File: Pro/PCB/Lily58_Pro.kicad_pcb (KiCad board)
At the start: 2 copper layers, 142.5 x 106.3 mm, 87 parts, among them J1 LED, J2 4PIN, J3 OLED, P1 i2c_pin, P2 i2c_pin, SW1 SW_PUSH, SW10 SW_PUSH, SW11 SW_PUSH, SW12 SW_PUSH, SW13 SW_PUSH, SW14 SW_PUSH, SW15 SW_PUSH, SW16 SW_PUSH, SW17 SW_PUSH, SW18 SW_PUSH, SW19 SW_PUSH, SW2 SW_PUSH, SW20 SW_PUSH, SW21 SW_PUSH, SW22 SW_PUSH, SW23 SW_PUSH, SW24 SW_PUSH, SW25 SW_PUSH, SW26 SW_PUSH, SW27 SW_PUSH, SW28 SW_PUSH, SW29 SW_PUSH, SW3 SW_PUSH, SW4 SW_PUSH, SW5 SW_PUSH, SW6 SW_PUSH, SW7 SW_PUSH, SW8 SW_PUSH, SW9 SW_PUSH, U1 ProMicro

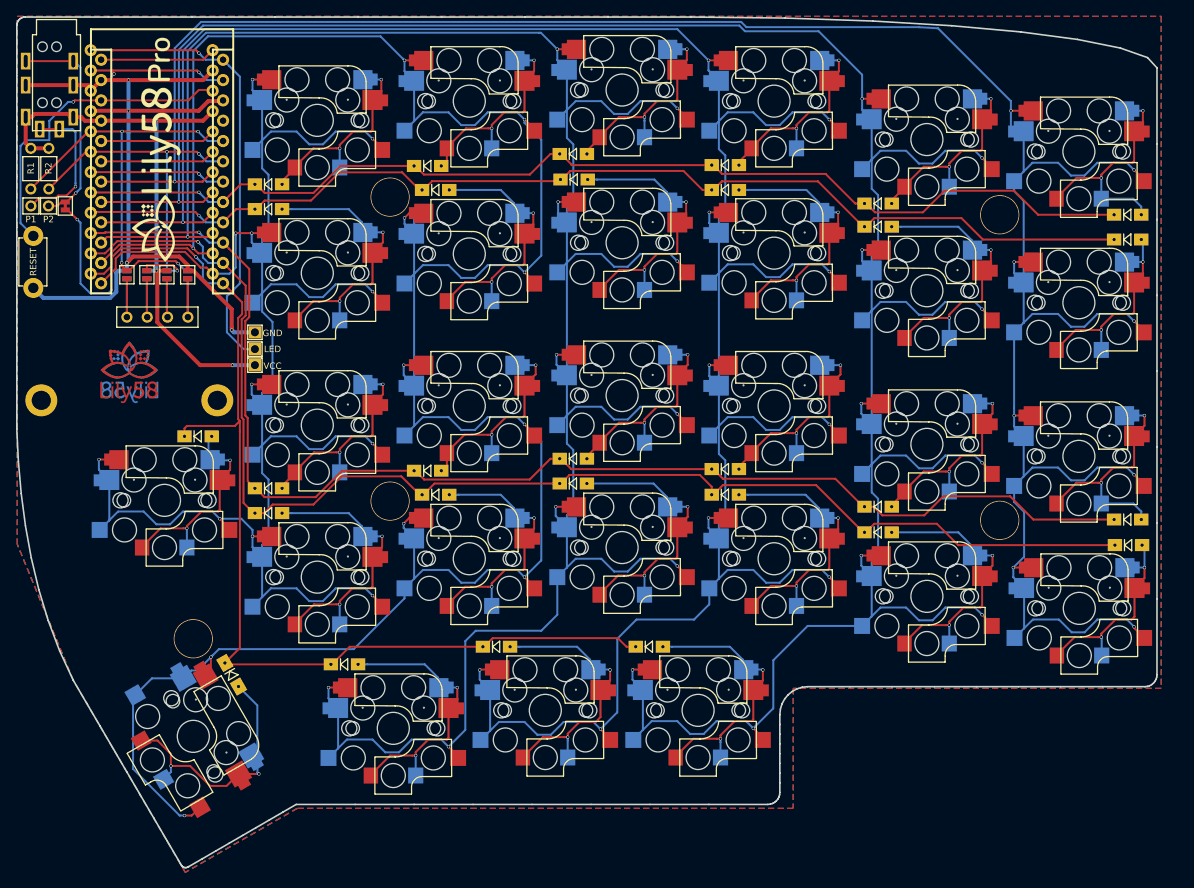
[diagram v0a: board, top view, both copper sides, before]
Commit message: Update project according KiCAD 7
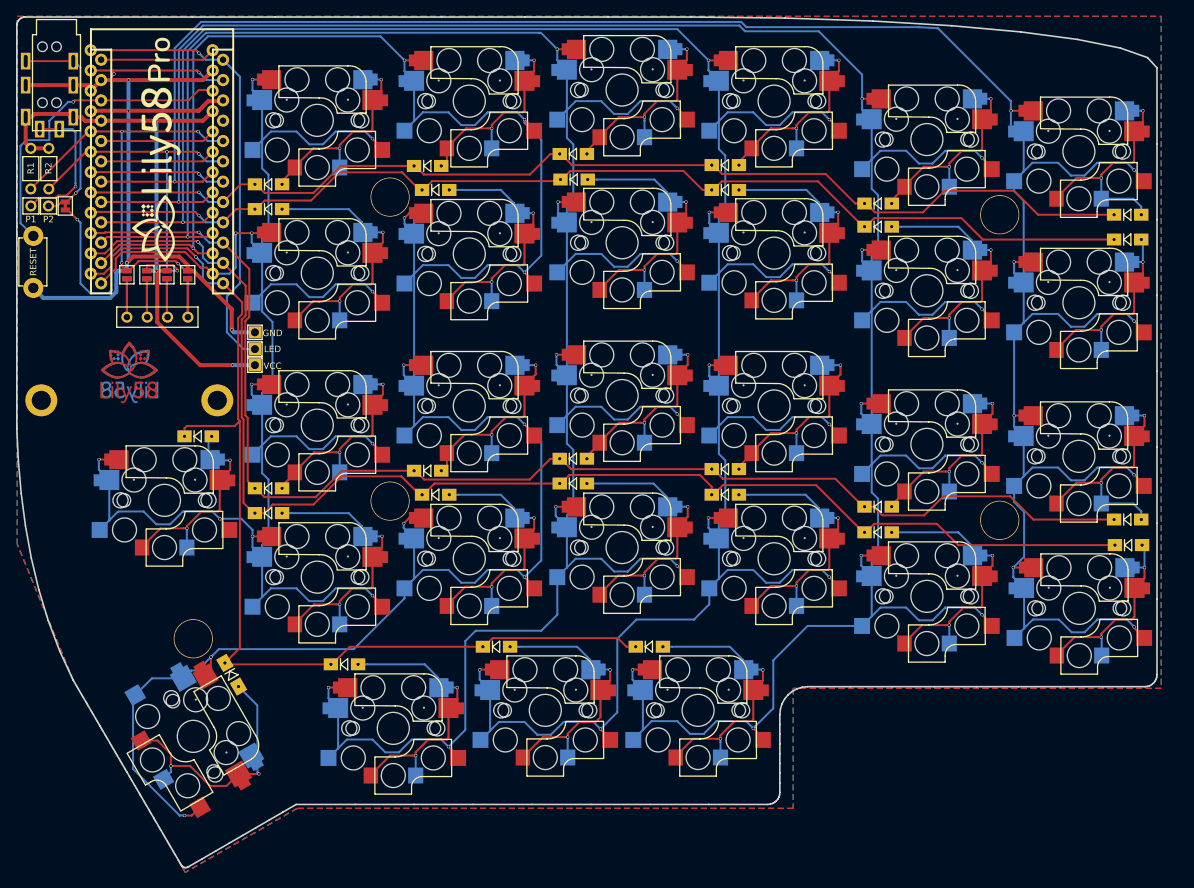
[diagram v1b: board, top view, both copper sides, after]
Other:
- net class Default removed
- net class GND removed
- net class VCC removed

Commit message: wireless scheme is almost ready
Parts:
- removed G*** (x2): LOGO, Lily58-footprint:lily58_logo_Pro
- removed G*** (x2): LOGO, Lily58-footprint:lily58_logo_2
- removed P1, P2: i2c_pin, Lily58-footprint:1pin_conn
- removed R1, R2: R, Lily58-footprint:RESISTOR_mini
- removed W1: jumper, Lily58-footprint:jumper_data
- added JP10: ~, Lily58_Pro:Jumper, B.Cu at (87.6, 61.6)
- added JP11: ~, Lily58_Pro:Jumper, F.Cu at (87.6, 61.6)
- added JP12: ~, Lily58_Pro:Jumper, F.Cu at (85.6, 61.6)
- added JP9: ~, Lily58_Pro:Jumper, B.Cu at (85.6, 61.6)
- added SW30: FS_SW_SPDT, marbastlib-various:SW_MSK12C02-HB, F.Cu at (84.6, 53.7)
- added SW31: BS_SW_SPDT, marbastlib-various:SW_MSK12C02-HB, B.Cu at (84.6, 53.7)
- D1, D10, D11, D12, D13, D14, D15, D16, D17, D18, D19, D2, D20, D21, D22, D23, D24, D25, D26, D27, D28, D29, D3, D4, D5, D6, D7, D8, D9: footprint Lily58-footprint:Diode_SOD123 -> Lily58_Pro:Diode_TH_SOD123
- J1: value LED -> FS_Battery_Socket; footprint Lily58-footprint:LED -> Connector_JST:JST_PH_S2B-PH-K_1x02_P2.00mm_Horizontal
- J2: value 4PIN -> BS_Battery_Socket; footprint Lily58-footprint:MJ-4PP-9 -> Connector_JST:JST_PH_S2B-PH-K_1x02_P2.00mm_Horizontal; moved to B.Cu
- J3: footprint Lily58-footprint:OLED_4Pin -> Lily58_Pro:OLED_4Pin
- JP1, JP2, JP3, JP4, JP5, JP6, JP7, JP8: value (none) -> Jumper_NO_Small; footprint Lily58-footprint:Jumper -> Lily58_Pro:Jumper
- RSW1: footprint Lily58-footprint:TACT_SWITCH_TVBP06 -> Lily58_Pro:TACT_SWITCH_TVBP06
- SW1, SW10, SW11, SW12, SW13, SW14, SW15, SW16, SW17, SW18, SW19, SW2, SW20, SW21, SW22, SW23, SW24, SW25, SW26, SW27, SW28, SW29, SW3, SW4, SW5, SW6, SW7, SW8, SW9: footprint Lily58-footprint:CherryMX_KailhLowProfile_Hotswap_edge -> Lily58_Pro:MX_Choc_Hotswap
- TH1, TH2: footprint Lily58-footprint:M2_HOLE_PCB -> Lily58_Pro:HOLE_M2
- TH3, TH4, TH5, TH6, TH7: footprint Lily58-footprint:HOLE_M2_TH -> Lily58_Pro:HOLE_M2_TH
- U1: footprint Lily58-footprint:ProMicro_rev2 -> Lily58_Pro:ProMicro_rev2
- moved J1 31.8 mm to (85.6, 64.5), turned to 0 degrees
- moved J2 25.2 mm to (87.6, 64.5), turned to 180 degrees
- moved RSW1 24.1 mm to (85.9, 43.6), turned to -90 degrees
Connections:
- J1 pad 1: VCC -> Net-(J1-Pin_1)
- J1 pad 2: LED -> Net-(J1-Pin_1)
- J2 pad 1: VCC -> Net-(J1-Pin_1)
- J2 pad 2: GND -> Net-(J1-Pin_1)
- U1 pad 1: LED -> unconnected-(U1-TX(PD3)-Pad1)
- U1 pad 19: Net-(U1-Pad19) -> unconnected-(U1-A2(PF5)-Pad19)
- U1 pad 20: Net-(U1-Pad20) -> unconnected-(U1-A3(PF4)-Pad20)
- U1 pad 24: Net-(U1-Pad24) -> RAW
- U1 pad 7: Net-(U1-Pad7) -> unconnected-(U1-D4(PD4)-Pad7)
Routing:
- net (no net): track 0.00 -> 414.3 mm, vias 0 -> 23
- net LED: track 57.0 -> 0.00 mm, vias 1 -> 0
- net DATA: track 59.7 -> 17.0 mm, vias 3 -> 1
- net Net-(D7-A): track 37.3 -> 0.00 mm, vias 2 -> 0
- net Net-(D19-A): track 37.2 -> 0.00 mm, vias 2 -> 0
- net Net-(D21-A): track 37.2 -> 0.00 mm, vias 2 -> 0
- net Net-(D23-A): track 37.1 -> 0.00 mm, vias 2 -> 0
- net Net-(D28-A): track 37.1 -> 0.00 mm, vias 2 -> 0
- net Net-(D22-A): track 37.1 -> 0.00 mm, vias 2 -> 0
- net Net-(D11-A): track 37.1 -> 0.00 mm, vias 2 -> 0
- net Net-(D10-A): track 37.0 -> 0.00 mm, vias 2 -> 0
- net VCC: track 72.9 -> 35.9 mm, vias 3 -> 2
- net Net-(D9-A): track 36.9 -> 0.00 mm, vias 2 -> 0
- net RAW: track 0.00 -> 36.9 mm, vias 0 -> 1
- net Net-(D8-A): track 35.0 -> 0.00 mm, vias 2 -> 0
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- removed copper zone on B.Cu, net GND
- removed copper zone on F.Cu, net GND
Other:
- outline, holes or cut-outs redrawn

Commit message: itermediate version
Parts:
- added G***: LOGO, Lily58_Pro:Hedgehog, B.Cu at (95.8, 82.0)
- added LOGO: LOGO, Lily58_Pro:Hedgehog, F.Cu at (95.8, 82.0)
- renumbered SW31 to B_Switch1, SW30 to F_Switch1, JP1 to JP_GND1, JP8 to JP_GND2, JP3 to JP_SCL1, JP6 to JP_SCL2, JP4 to JP_SDA1, JP5 to JP_SDA2, JP2 to JP_VCC1, JP7 to JP_VCC2
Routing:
- net (no net): track 414.3 -> 0.00 mm, vias 23 -> 0
- net Net-(D7-A): track 0.00 -> 37.3 mm, vias 0 -> 2
- net Net-(D19-A): track 0.00 -> 37.2 mm, vias 0 -> 2
- net Net-(D21-A): track 0.00 -> 37.2 mm, vias 0 -> 2
- net Net-(D23-A): track 0.00 -> 37.1 mm, vias 0 -> 2
- net Net-(D28-A): track 0.00 -> 37.1 mm, vias 0 -> 2
- net Net-(D22-A): track 0.00 -> 37.1 mm, vias 0 -> 2
- net Net-(D11-A): track 0.00 -> 37.1 mm, vias 0 -> 2
- net Net-(D10-A): track 0.00 -> 37.0 mm, vias 0 -> 2
- net Net-(D9-A): track 0.00 -> 36.9 mm, vias 0 -> 2
- net Net-(D8-A): track 0.00 -> 35.0 mm, vias 0 -> 2
- net Net-(D25-A): track 0.00 -> 28.2 mm, vias 0 -> 2
- net unconnected-(U1-D4(PD4)-Pad7): track 0.00 -> 17.0 mm, vias 0 -> 1

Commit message: It's done. v0.1 ready to print
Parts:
- D1, D10, D11, D12, D13, D14, D15, D16, D17, D18, D19, D2, D20, D21, D22, D23, D24, D25, D26, D27, D28, D29, D3, D4, D5, D6, D7, D8, D9: footprint Lily58_Pro:Diode_TH_SOD123 -> Hedgehog:Diode_SOD123
- renumbered LOGO to Hedgehog_v0.1, G*** to Hedgehog_v0.1
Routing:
- added copper zone on B.Cu, net GND
- added copper zone on F.Cu, net GND
